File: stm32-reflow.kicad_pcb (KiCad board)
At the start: 4 copper layers, 64 x 59 mm, 62 parts, among them J1 TC2030, J10 63824-1, J11 63824-1, J12 63824-1, J2 Conn_01x04_Male, J3 Conn_01x03_Male, J4 Screw_Terminal_01x02, J5 Screw_Terminal_01x02, J6 Conn_02x08_Odd_Even, J7 63824-1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

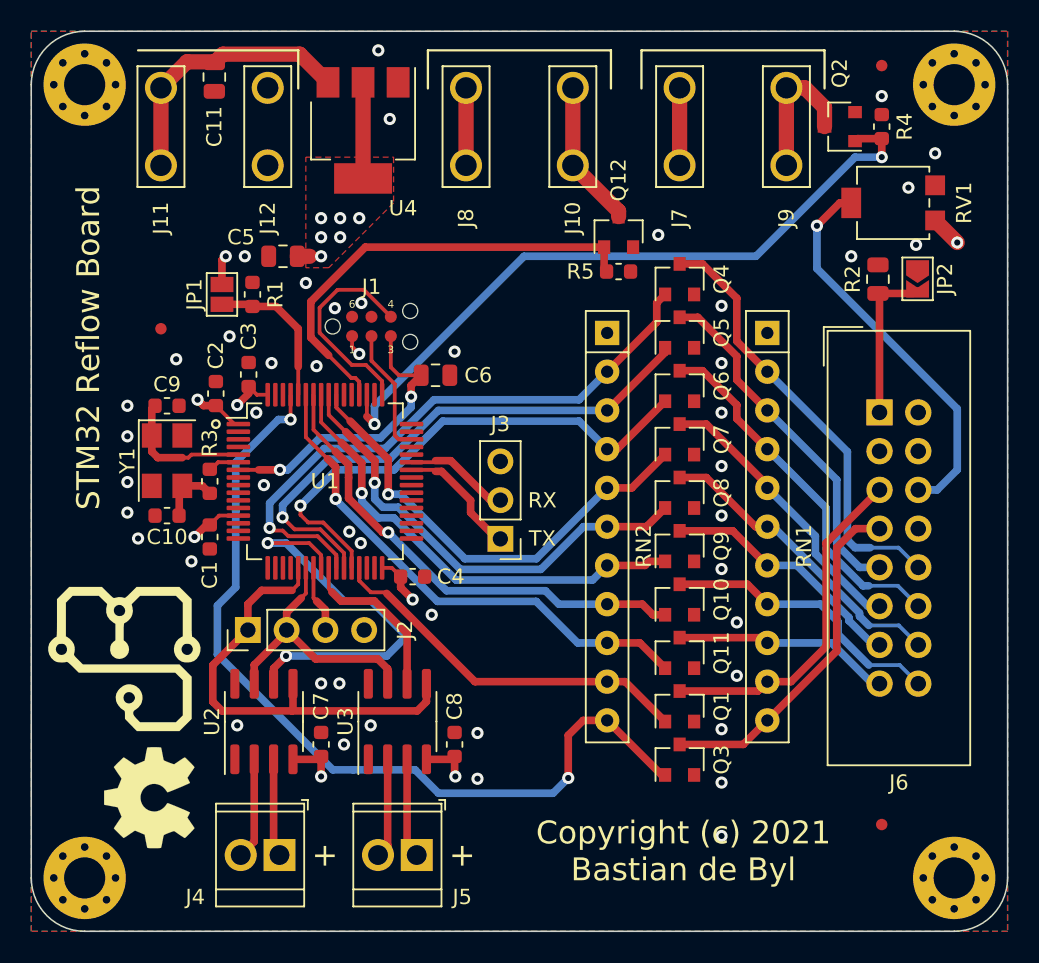
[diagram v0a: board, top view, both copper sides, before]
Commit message: added encoder interface
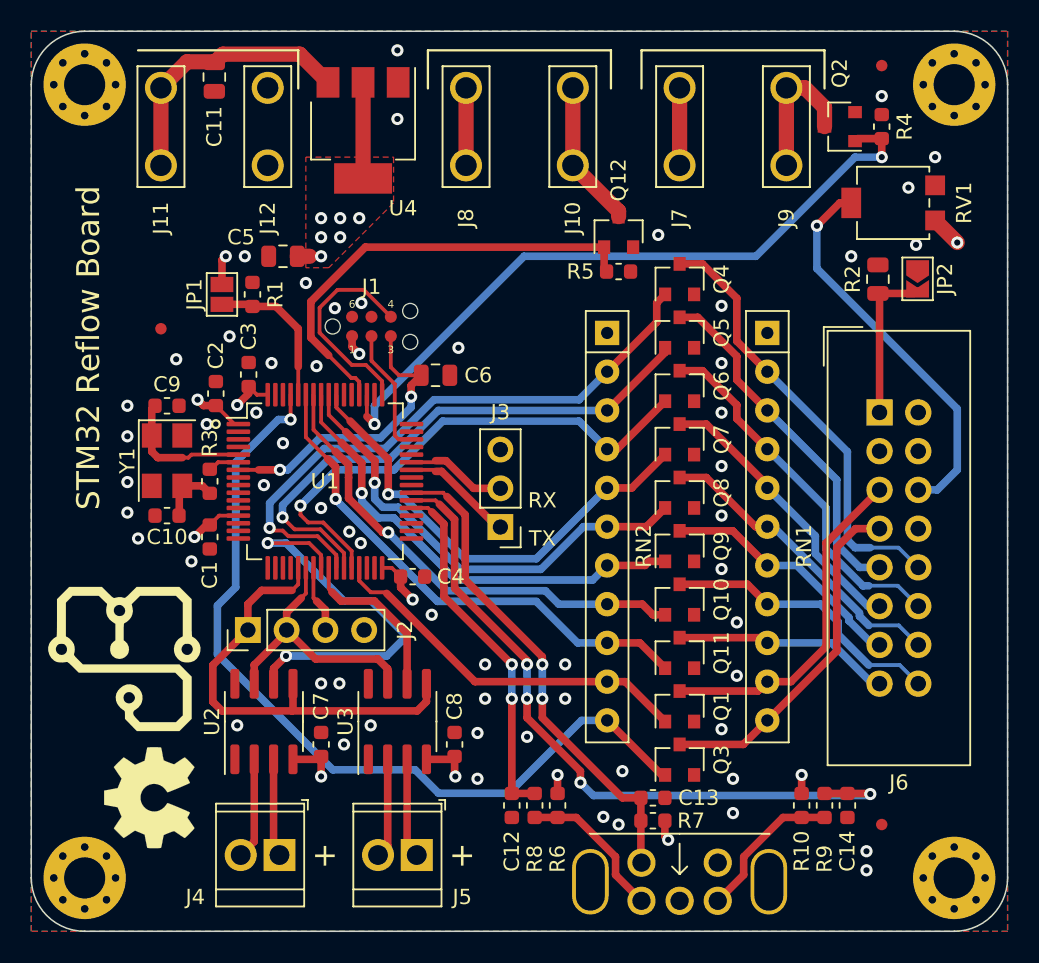
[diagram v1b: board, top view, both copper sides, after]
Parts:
- removed the REF** at (144.6, 120.6)
- added C12: 10n, Capacitor_SMD:C_0603_1608Metric, F.Cu at (143.0, 125.0)
- added C13: 10n, Capacitor_SMD:C_0603_1608Metric, F.Cu at (152.2, 124.5)
- added C14: 10n, Capacitor_SMD:C_0603_1608Metric, F.Cu at (165.0, 125.0)
- added R10: 10k, Resistor_SMD:R_0603_1608Metric, F.Cu at (162.0, 125.0)
- added R6: 10k, Resistor_SMD:R_0603_1608Metric, F.Cu at (146.0, 125.0)
- added R7: 10k, Resistor_SMD:R_0603_1608Metric, F.Cu at (152.2, 126.0)
- added R8: 10k, Resistor_SMD:R_0603_1608Metric, F.Cu at (144.5, 125.0)
- added R9: 10k, Resistor_SMD:R_0603_1608Metric, F.Cu at (163.5, 125.0)
- added SW1: EN11-VSM, Personal:EN11-VSM1AF20, F.Cu at (154.0, 130.0)
- moved J3 0.78 mm to (142.2, 106.8)
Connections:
- U1 pad 37: unconnected-(U1-Pad37) -> /Reflow MCU/ENC_A
- U1 pad 38: unconnected-(U1-Pad38) -> /Reflow MCU/ENC_B
- U1 pad 39: unconnected-(U1-Pad39) -> /Reflow MCU/ENC_SW
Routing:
- net /Reflow MCU/ENC_B: track 0.00 -> 46.4 mm, vias 0 -> 4
- net /Reflow MCU/ENC_SW: track 0.00 -> 32.4 mm, vias 0 -> 2
- net /Reflow MCU/ENC_A: track 0.00 -> 23.6 mm, vias 0 -> 2
- net Net-(R6-Pad2): track 0.00 -> 9.96 mm
- net Net-(R10-Pad1): track 0.00 -> 9.96 mm
- net +3V3: track 30.0 -> 33.7 mm, vias 14 -> 17
- net /Reflow Level Shifting/E: track 57.7 -> 56.1 mm, vias 2 -> 1
- net /Reflow MCU/USART1_TX: track 8.17 -> 7.38 mm
- net GND: vias 46 -> 59
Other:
- board text removed: "Copyright (c) 2021 Bastian de Byl"

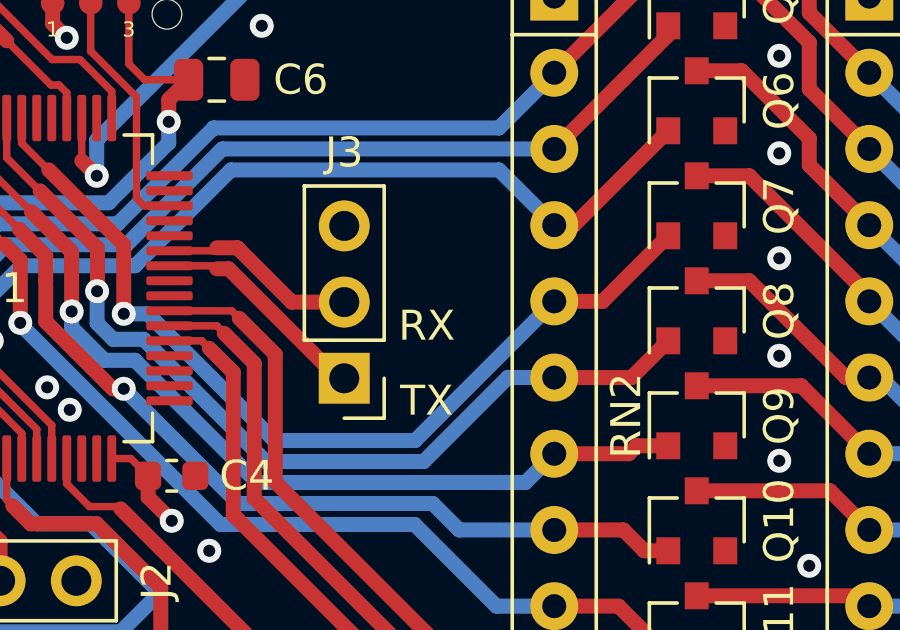
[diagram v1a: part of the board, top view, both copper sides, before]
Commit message: organized schematic more, fixed net naming of rw
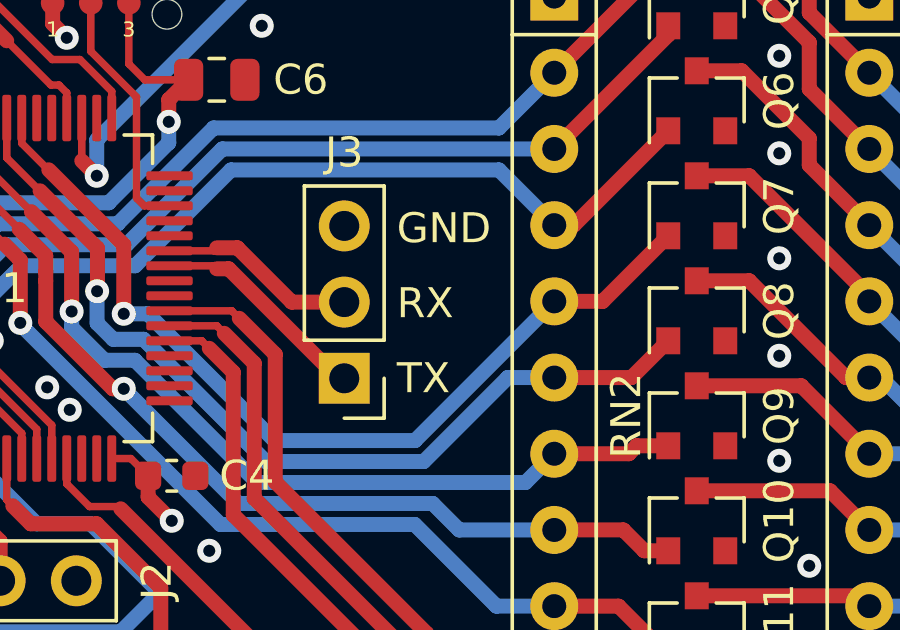
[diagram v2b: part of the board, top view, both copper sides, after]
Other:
- board text added: "GND"
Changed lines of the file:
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@@
     (pad "" thru_hole oval (at 5.85 0) (size 2.4 4.3) (drill oval 1.9 3.8) (layers *.Cu *.Mask))
     (pad "A" thru_hole circle (at -2.5 1.25) (size 1.85 1.85) (drill 1.2) (layers *.Cu *.Mask)
-      (net 81 "Net-(R6-Pad2)") (pinfunction "A"))
+      (net 81 "Net-(R6-Pad2)") (pinfunction "A") (pintype "passive"))
     (pad "B" thru_hole circle (at 2.5 1.25) (size 1.85 1.85) (drill 1.2) (layers *.Cu *.Mask)
-      (net 82 "Net-(R10-Pad1)") (pinfunction "B"))
+      (net 82 "Net-(R10-Pad1)") (pinfunction "B") (pintype "passive"))
     (pad "C" thru_hole circle (at 0 1.25) (size 1.85 1.85) (drill 1.2) (layers *.Cu *.Mask)
-      (net 2 "GND") (pinfunction "C"))
+      (net 2 "GND") (pinfunction "C") (pintype "passive"))
     (pad "S1" thru_hole circle (at -2.5 -1.25) (size 1.85 1.85) (drill 1.2) (layers *.Cu *.Mask)
-      (net 45 "/Reflow MCU/ENC_SW") (pinfunction "S1"))
+      (net 45 "/Reflow MCU/ENC_SW") (pinfunction "S1") (pintype "passive"))
     (pad "S2" thru_hole circle (at 2.5 -1.25) (size 1.85 1.85) (drill 1.2) (layers *.Cu *.Mask)
-      (net 2 "GND") (pinfunction "S2"))
+      (net 2 "GND") (pinfunction "S2") (pintype "passive"))
     (model "${KISYS3DMOD}/Button_Switch_THT.3dshapes/EN11-VSM.wrl"
       (offset (xyz 6 -1.75 14))
@@
     (effects (font (size 1.5 1.5) (thickness 0.3)) (justify mirror))
   )
-  (gr_text "RX" (at 145 105) (layer "F.SilkS")
-    (effects (font (size 1 1) (thickness 0.15)))
+  (gr_text "RX" (at 144 104.25) (layer "F.SilkS")
+    (effects (font (size 1 1) (thickness 0.15)) (justify left))
   )
   (gr_text "+" (at 130.75 128.25) (layer "F.SilkS")
     (effects (font (size 1.5 1.5) (thickness 0.3)))
   )
-  (gr_text "TX" (at 145 107.5) (layer "F.SilkS")
-    (effects (font (size 1 1) (thickness 0.15)))
+  (gr_text "GND" (at 144 101.75) (layer "F.SilkS")
+    (effects (font (size 1 1) (thickness 0.15)) (justify left))
+  )
+  (gr_text "TX" (at 144 106.75) (layer "F.SilkS")
+    (effects (font (size 1 1) (thickness 0.15)) (justify left))
   )
   (gr_text "+" (at 139.750001 128.25) (layer "F.SilkS")

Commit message: finalized design for production
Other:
- board text added: "JLCJLCJLCJLC"
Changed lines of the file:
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@@
     (effects (font (size 1 1) (thickness 0.2)) (justify right mirror))
+  )
+  (gr_text "JLCJLCJLCJLC" (at 142 86.75) (layer "B.SilkS")
+    (effects (font (size 1 1) (thickness 0.15)) (justify mirror))
   )
   (gr_text "VCC" (at 166 101.75) (layer "B.SilkS")

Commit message: added revision label, finalized for fabrication
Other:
- board text added: "rev. 07684a7"
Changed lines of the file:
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@@
     (effects (font (size 1 1) (thickness 0.15)) (justify left))
+  )
+  (gr_text "rev. 07684a7" (at 117.75 91 90) (layer "F.SilkS")
+    (effects (font (size 1 1) (thickness 0.15)))
   )
   (gr_text "TX" (at 144 106.75) (layer "F.SilkS")

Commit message: updated bom to reflect non-backordered parts
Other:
- board text removed: "JLCJLCJLCJLC"
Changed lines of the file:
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@@
       (outputformat 1)
       (mirror false)
-      (drillshape 1)
+      (drillshape 0)
       (scaleselection 1)
-      (outputdirectory "")
+      (outputdirectory "fabrication/")
     )
   )
@@
     (effects (font (size 1 1) (thickness 0.2)) (justify right mirror))
   )
-  (gr_text "JLCJLCJLCJLC" (at 142 86.75) (layer "B.SilkS")
-    (effects (font (size 1 1) (thickness 0.15)) (justify mirror))
-  )
   (gr_text "VCC" (at 166 101.75) (layer "B.SilkS")
